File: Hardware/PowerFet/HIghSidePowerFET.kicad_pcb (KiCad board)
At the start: 2 copper layers, 44.6 x 52.4 mm, 32 parts, among them J1 Conn_01x02, U1 TPS4810-Q1, U2 LTV-356T

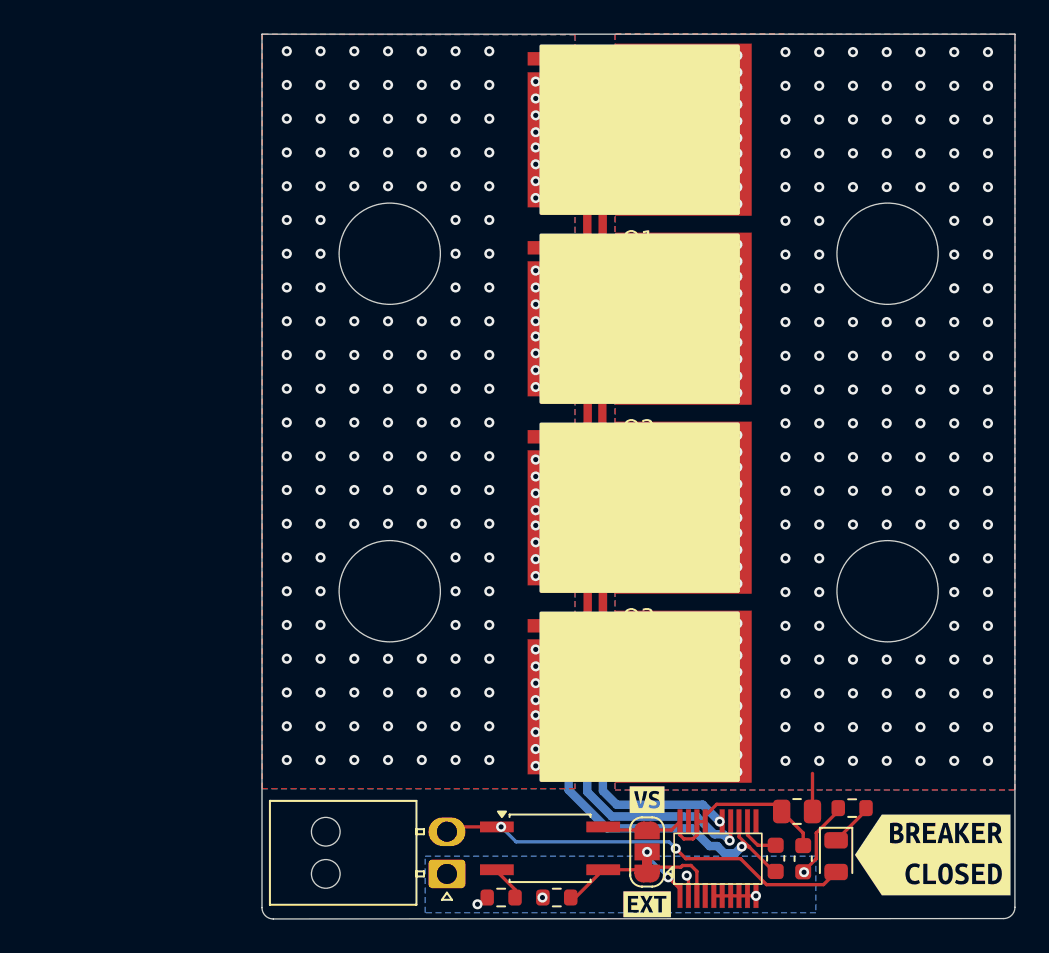
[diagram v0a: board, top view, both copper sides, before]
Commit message: BMS updates, power/fet final updates
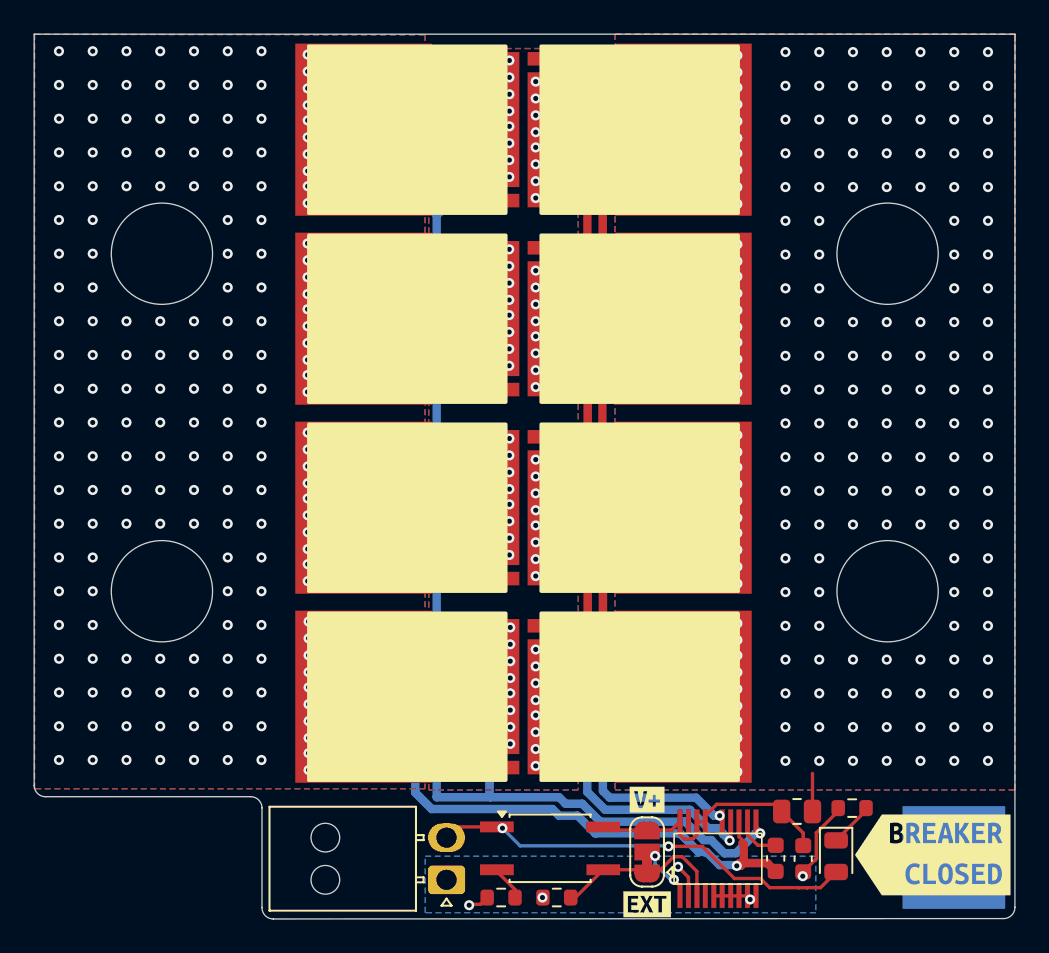
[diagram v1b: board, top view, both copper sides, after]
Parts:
- removed kibuzzard-68F79DB8: G***, kibuzzard-68F79DB8
- removed kibuzzard-68F7ACD6: G***, kibuzzard-68F7ACD6
- removed kibuzzard-68F7AD8A: G***, kibuzzard-68F7AD8A
- removed kibuzzard-68F7ADA7: G***, kibuzzard-68F7ADA7
- added G*** (x2): LOGO, LOGO, B.Cu at (179.6, 122.1)
- added G***: LOGO, LOGO, B.Cu at (154.2, 107.9)
- added G***: LOGO, LOGO, B.Cu at (179.5, 122.3)
- added G***: LOGO, LOGO, B.Cu at (150.6, 103.9)
- added Q2: ~, BAD_LIB:NTBLS0D8N08X, F.Cu at (148.6, 79.2)
- added Q3: ~, BAD_LIB:NTBLS0D8N08X, F.Cu at (159.4, 90.3)
- added Q6: ~, BAD_LIB:NTBLS0D8N08X, F.Cu at (148.6, 101.5)
- added Q7: ~, BAD_LIB:NTBLS0D8N08X, F.Cu at (159.4, 112.8)
- added kibuzzard-6906AA9C: G***, kibuzzard-6906AA9C, B.Cu at (154.1, 84.6)
- added kibuzzard-6906AD14: G***, kibuzzard-6906AD14, B.Cu at (154.1, 78.0)
- added kibuzzard-6906C7DA: G***, kibuzzard-6906C7DA, B.Cu at (171.1, 124.4)
- added kibuzzard-6906CB2D: G***, kibuzzard-6906CB2D, F.Cu at (161.3, 118.8)
- added kibuzzard-690797E2: G***, kibuzzard-690797E2, B.Cu at (160.3, 122.4)
- added kibuzzard-6907FFCC: G***, kibuzzard-6907FFCC, B.Cu at (172.3, 120.1)
- added kibuzzard-6907FFEA: G***, kibuzzard-6907FFEA, B.Cu at (173.6, 122.3)
- Q1: footprint OlinBAD:NTBLS0D8N08X -> BAD_LIB:NTBLS0D8N08X
- Q4: renamed from Q2; footprint OlinBAD:NTBLS0D8N08X -> BAD_LIB:NTBLS0D8N08X
- Q5: renamed from Q3; footprint OlinBAD:NTBLS0D8N08X -> BAD_LIB:NTBLS0D8N08X
- Q8: renamed from Q4; footprint OlinBAD:NTBLS0D8N08X -> BAD_LIB:NTBLS0D8N08X
- moved Q4 10.8 mm to (148.6, 90.3), turned to 180 degrees
- moved Q8 10.8 mm to (148.6, 112.8), turned to 180 degrees
- moved kibuzzard-68F7A12F 0.36 mm to (153.7, 122.3)
- moved kibuzzard-68F7A0AD 0.36 mm to (151.9, 123.5)
- moved kibuzzard-68F7A0C5 0.36 mm to (151.9, 120.8)
- moved J1 0.35 mm to (149.5, 123.6)
- renumbered R12 to R1, R5 to R11, R11 to R12, R7 to R2, R6 to R3, R1 to R4, R2 to R5, R8 to R6, R3 to R7, R9 to R8, R4 to R9
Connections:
- Q1 pad 2: /CORE+ -> /DIODE+
- Q4 pad 1: Net-(Q2-G) -> /G2
- Q4 pad 2: /CORE+ -> /DIODE+
- Q4 pad 3: /BATT+ -> /CORE+
- Q5 pad 2: /CORE+ -> /DIODE+
- Q8 pad 1: Net-(Q4-G) -> /G2
- Q8 pad 2: /CORE+ -> /DIODE+
- Q8 pad 3: /BATT+ -> /CORE+
- R11 pad 1: Net-(Q4-G) -> Net-(Q7-G)
- R12 pad 2: Net-(Q4-G) -> Net-(Q7-G)
- R7 pad 1: Net-(Q2-G) -> Net-(Q3-G)
- R8 pad 2: Net-(Q2-G) -> Net-(Q3-G)
- U1 pad 11: unconnected-(U1-G2-Pad11) -> /G2
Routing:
- net /G2: track 0.00 -> 67.7 mm, vias 0 -> 5
- net /CORE+: track 16.8 -> 27.6 mm, vias 233 -> 453
- net Net-(Q3-G): track 0.00 -> 5.60 mm, vias 0 -> 1
- net Net-(Q2-G): track 5.60 -> 0.00 mm, vias 1 -> 0
- net Net-(Q7-G): track 0.00 -> 5.59 mm, vias 0 -> 1
- net Net-(Q4-G): track 5.59 -> 0.00 mm, vias 1 -> 0
- net GND: track 9.20 -> 10.6 mm
- net /DIODE+: vias 0 -> 192
- net /BATT+: vias 456 -> 455
- added copper zone on B.Cu, net /DIODE+
- added copper zone on F.Cu, net /DIODE+
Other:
- board size 44.6 x 52.4 mm -> 58.1 x 52.4 mm
